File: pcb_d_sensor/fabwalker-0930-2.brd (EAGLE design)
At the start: 22.3 x 27.9 mm, 11 parts

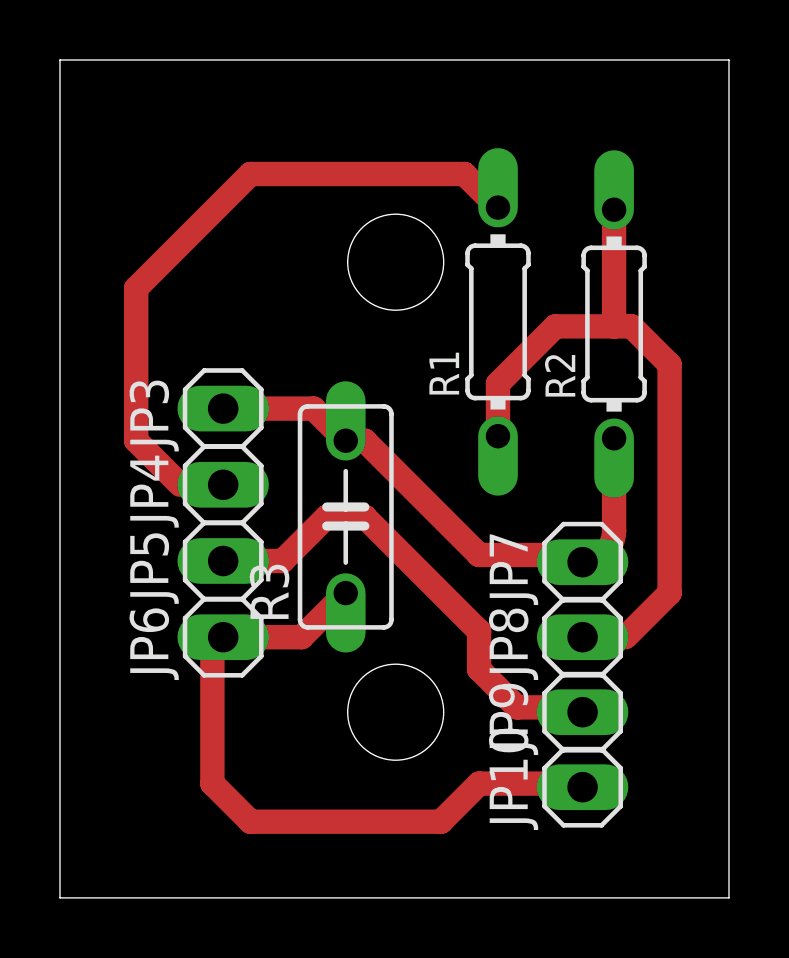
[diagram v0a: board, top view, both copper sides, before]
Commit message: 干渉を避けるためネジ穴の位置を修正
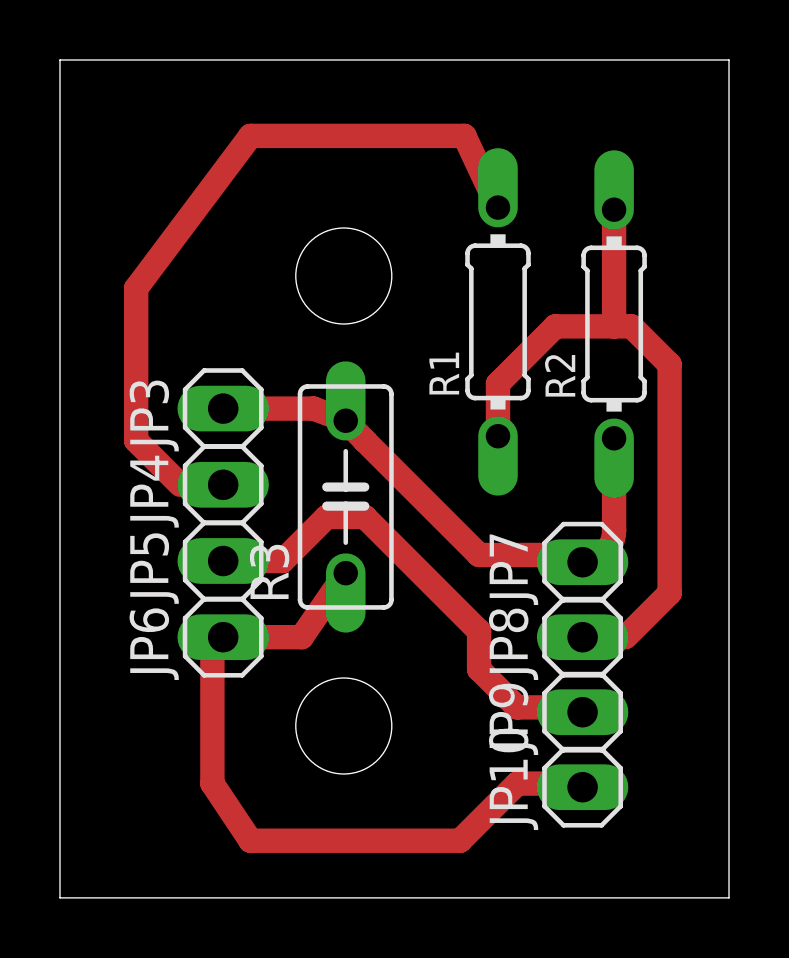
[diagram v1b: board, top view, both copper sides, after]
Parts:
- moved R3 0.66 mm to (12.1, 14.6)
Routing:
- net N$2: track 22.7 -> 24.7 mm
- net N$4: track 23.2 -> 24.4 mm
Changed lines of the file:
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@@
 <setting verticaltext="up"/>
 </settings>
-<grid distance="0.05" unitdist="inch" unit="inch" style="lines" multiple="1" display="yes" altdistance="0.025" altunitdist="inch" altunit="inch"/>
+<grid distance="1" unitdist="mm" unit="mm" style="lines" multiple="1" display="yes" altdistance="0.025" altunitdist="inch" altunit="inch"/>
 <layers>
 <layer number="1" name="Top" color="4" fill="1" visible="yes" active="yes"/>
@@
 <layer number="27" name="tValues" color="7" fill="1" visible="yes" active="yes"/>
 <layer number="28" name="bValues" color="7" fill="1" visible="yes" active="yes"/>
-<layer number="29" name="tStop" color="7" fill="3" visible="no" active="yes"/>
-<layer number="30" name="bStop" color="7" fill="6" visible="no" active="yes"/>
-<layer number="31" name="tCream" color="7" fill="4" visible="no" active="yes"/>
-<layer number="32" name="bCream" color="7" fill="5" visible="no" active="yes"/>
-<layer number="33" name="tFinish" color="6" fill="3" visible="no" active="yes"/>
-<layer number="34" name="bFinish" color="6" fill="6" visible="no" active="yes"/>
-<layer number="35" name="tGlue" color="7" fill="4" visible="no" active="yes"/>
-<layer number="36" name="bGlue" color="7" fill="5" visible="no" active="yes"/>
-<layer number="37" name="tTest" color="7" fill="1" visible="no" active="yes"/>
-<layer number="38" name="bTest" color="7" fill="1" visible="no" active="yes"/>
-<layer number="39" name="tKeepout" color="4" fill="11" visible="no" active="yes"/>
-<layer number="40" name="bKeepout" color="1" fill="11" visible="no" active="yes"/>
-<layer number="41" name="tRestrict" color="4" fill="10" visible="no" active="yes"/>
-<layer number="42" name="bRestrict" color="1" fill="10" visible="no" active="yes"/>
-<layer number="43" name="vRestrict" color="2" fill="10" visible="no" active="yes"/>
-<layer number="44" name="Drills" color="7" fill="1" visible="no" active="yes"/>
-<layer number="45" name="Holes" color="7" fill="1" visible="no" active="yes"/>
-<layer number="46" name="Milling" color="3" fill="1" visible="no" active="yes"/>
-<layer number="47" name="Measures" color="7" fill="1" visible="no" active="yes"/>
+<layer number="29" name="tStop" color="7" fill="3" visible="yes" active="yes"/>
+<layer number="30" name="bStop" color="7" fill="6" visible="yes" active="yes"/>
+<layer number="31" name="tCream" color="7" fill="4" visible="yes" active="yes"/>
+<layer number="32" name="bCream" color="7" fill="5" visible="yes" active="yes"/>
+<layer number="33" name="tFinish" color="6" fill="3" visible="yes" active="yes"/>
+<layer number="34" name="bFinish" color="6" fill="6" visible="yes" active="yes"/>
+<layer number="35" name="tGlue" color="7" fill="4" visible="yes" active="yes"/>
+<layer number="36" name="bGlue" color="7" fill="5" visible="yes" active="yes"/>
+<layer number="37" name="tTest" color="7" fill="1" visible="yes" active="yes"/>
+<layer number="38" name="bTest" color="7" fill="1" visible="yes" active="yes"/>
+<layer number="39" name="tKeepout" color="4" fill="11" visible="yes" active="yes"/>
+<layer number="40" name="bKeepout" color="1" fill="11" visible="yes" active="yes"/>
+<layer number="41" name="tRestrict" color="4" fill="10" visible="yes" active="yes"/>
+<layer number="42" name="bRestrict" color="1" fill="10" visible="yes" active="yes"/>
+<layer number="43" name="vRestrict" color="2" fill="10" visible="yes" active="yes"/>
+<layer number="44" name="Drills" color="7" fill="1" visible="yes" active="yes"/>
+<layer number="45" name="Holes" color="7" fill="1" visible="yes" active="yes"/>
+<layer number="46" name="Milling" color="3" fill="1" visible="yes" active="yes"/>
+<layer number="47" name="Measures" color="7" fill="1" visible="yes" active="yes"/>
 <layer number="48" name="Document" color="7" fill="1" visible="no" active="yes"/>
 <layer number="49" name="Reference" color="7" fill="1" visible="no" active="yes"/>
@@
 <wire x1="24.84" y1="29.2" x2="2.54" y2="29.2" width="0" layer="20"/>
 <wire x1="2.54" y1="29.2" x2="2.54" y2="1.27" width="0" layer="20"/>
-<hole x="13.73" y="7.46" drill="3.2"/>
-<hole x="13.73" y="22.46" drill="3.2"/>
+<hole x="12" y="7" drill="3.2"/>
+<hole x="12" y="22" drill="3.2"/>
 <polygon width="0" layer="48">
 <vertex x="3.73" y="24.96"/>
@@
 <element name="R1" library="Yamaguchi" package="0204/7" value="RES_7MM" x="17.14" y="20.47" rot="R90"/>
 <element name="R2" library="Yamaguchi" package="0204/7" value="RES_7MM" x="21.01" y="20.4" rot="R90"/>
-<element name="R3" library="Yamaguchi" package="C050-030X075" value="CAP_5MM" x="12.065" y="13.97" rot="R90"/>
+<element name="R3" library="Yamaguchi" package="C050-030X075" value="CAP_5MM" x="12.065" y="14.635" rot="R90"/>
 </elements>
 <signals>
@@
 <wire x1="21.01" y1="13.51" x2="19.96" y2="12.46" width="0.8128" layer="1" curve="-90"/>
 <wire x1="7.98" y1="17.58" x2="10.995" y2="17.58" width="0.8128" layer="1"/>
-<wire x1="10.995" y1="17.58" x2="12.065" y2="16.51" width="0.8128" layer="1"/>
-<wire x1="12.065" y1="16.51" x2="12.7" y2="16.51" width="0.8128" layer="1"/>
+<wire x1="10.995" y1="17.58" x2="12.065" y2="17.175" width="0.8128" layer="1"/>
+<wire x1="12.065" y1="17.175" x2="12.7" y2="16.51" width="0.8128" layer="1"/>
 <wire x1="12.7" y1="16.51" x2="16.51" y2="12.7" width="0.8128" layer="1"/>
 <wire x1="16.51" y1="12.7" x2="19.72" y2="12.7" width="0.8128" layer="1"/>
@@
 <wire x1="6.55" y1="15.04" x2="5.08" y2="16.51" width="0.8128" layer="1"/>
 <wire x1="5.08" y1="16.51" x2="5.08" y2="21.59" width="0.8128" layer="1"/>
-<wire x1="5.08" y1="21.59" x2="8.89" y2="25.4" width="0.8128" layer="1"/>
-<wire x1="8.89" y1="25.4" x2="16.02" y2="25.4" width="0.8128" layer="1"/>
-<wire x1="16.02" y1="25.4" x2="17.14" y2="24.28" width="0.8128" layer="1"/>
+<wire x1="5.08" y1="21.59" x2="8.89" y2="26.67" width="0.8128" layer="1"/>
+<wire x1="8.89" y1="26.67" x2="16.02" y2="26.67" width="0.8128" layer="1"/>
+<wire x1="16.02" y1="26.67" x2="17.14" y2="24.28" width="0.8128" layer="1"/>
 </signal>
 <signal name="N$4">
@@
 <contactref element="JP10" pad="1"/>
 <wire x1="19.84" y1="5.08" x2="19.96" y2="4.96" width="0.4064" layer="1"/>
-<wire x1="19.84" y1="5.08" x2="16.51" y2="5.08" width="0.8128" layer="1"/>
-<wire x1="16.51" y1="5.08" x2="15.24" y2="3.81" width="0.8128" layer="1"/>
-<wire x1="15.24" y1="3.81" x2="8.89" y2="3.81" width="0.8128" layer="1"/>
-<wire x1="8.89" y1="3.81" x2="7.62" y2="5.08" width="0.8128" layer="1"/>
+<wire x1="19.84" y1="5.08" x2="17.78" y2="5.08" width="0.8128" layer="1"/>
+<wire x1="17.78" y1="5.08" x2="15.875" y2="3.175" width="0.8128" layer="1"/>
+<wire x1="15.875" y1="3.175" x2="8.89" y2="3.175" width="0.8128" layer="1"/>
+<wire x1="8.89" y1="3.175" x2="7.62" y2="5.08" width="0.8128" layer="1"/>
 <wire x1="7.62" y1="5.08" x2="7.62" y2="9.6" width="0.8128" layer="1"/>
 <wire x1="7.62" y1="9.6" x2="7.98" y2="9.96" width="0.8128" layer="1"/>
 <wire x1="7.98" y1="9.96" x2="10.595" y2="9.96" width="0.8128" layer="1"/>
-<wire x1="10.595" y1="9.96" x2="12.065" y2="11.43" width="0.8128" layer="1"/>
+<wire x1="10.595" y1="9.96" x2="12.065" y2="12.095" width="0.8128" layer="1"/>
 </signal>
 <signal name="N$6">
